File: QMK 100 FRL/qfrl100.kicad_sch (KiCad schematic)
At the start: 18 parts

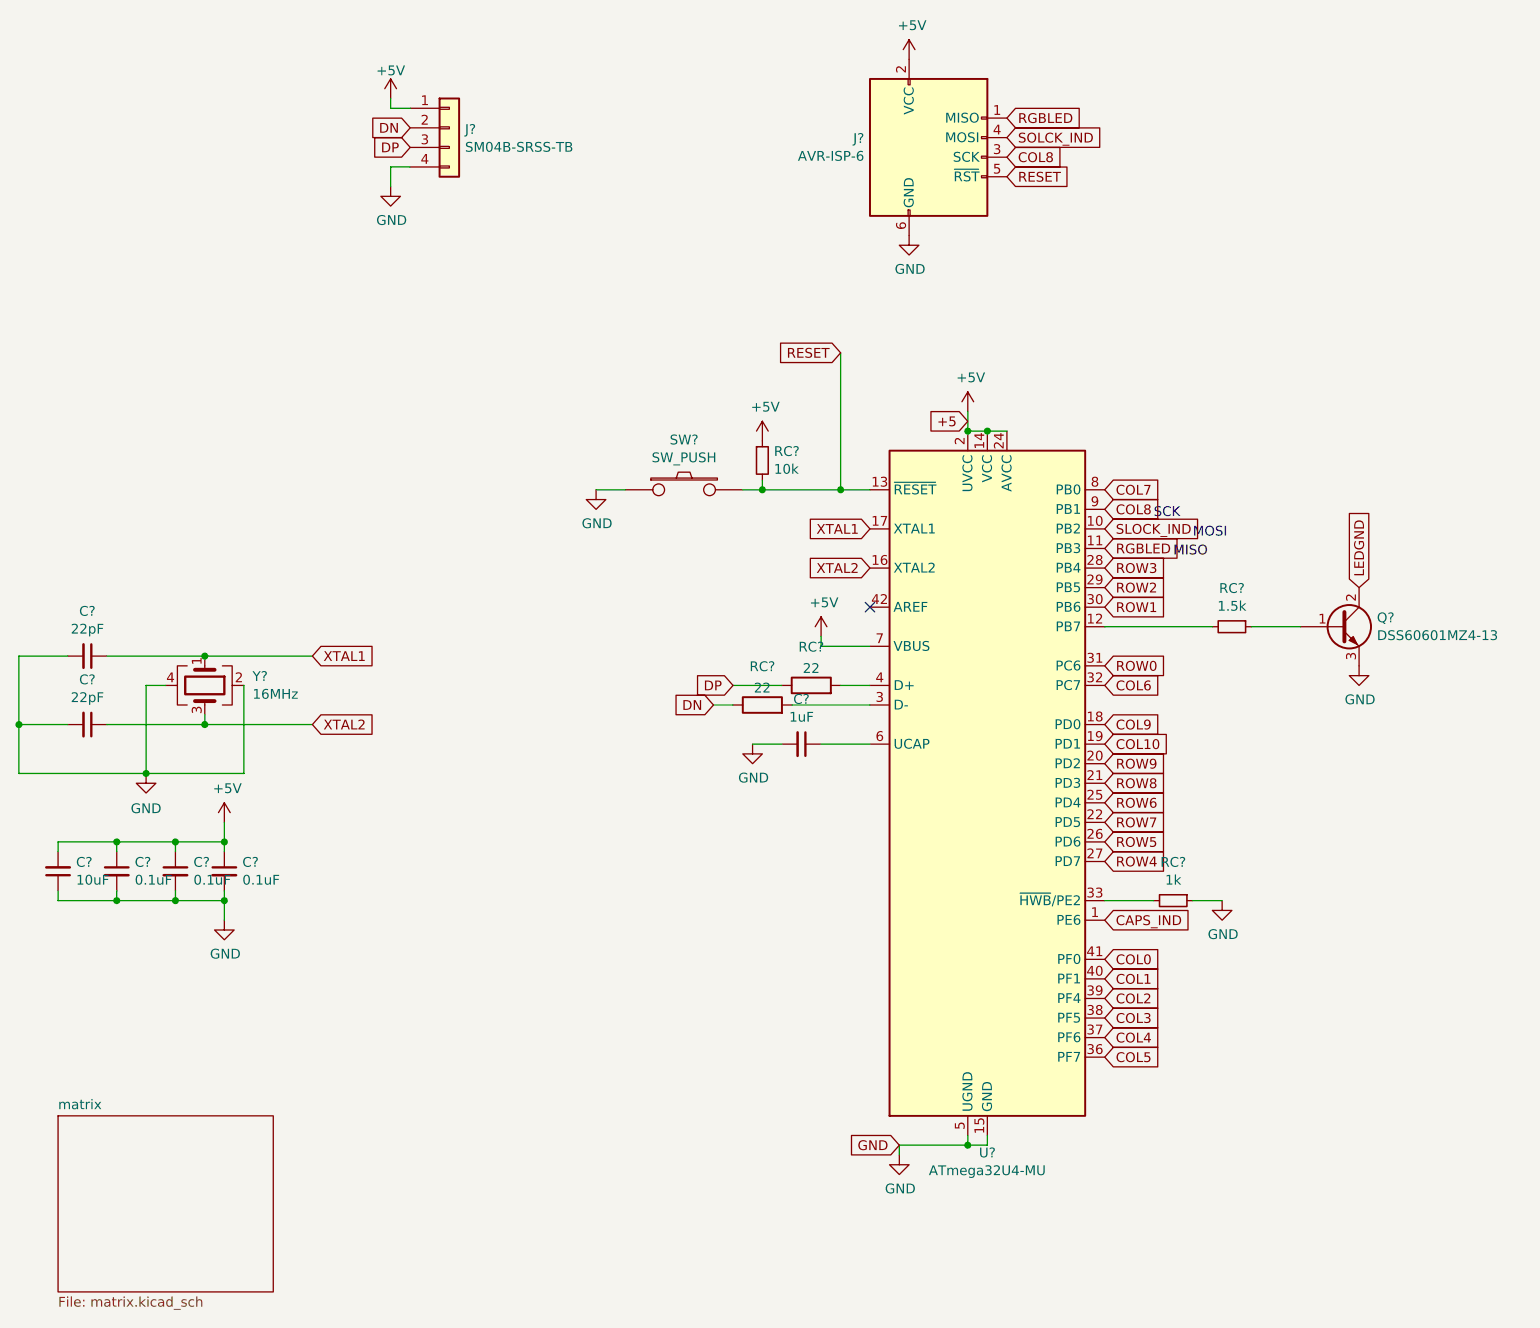
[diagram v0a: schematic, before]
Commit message: Finished from the first schema and pcb
Finished the schematics and foot prints links and updated the pcb foot prints to the pcb.
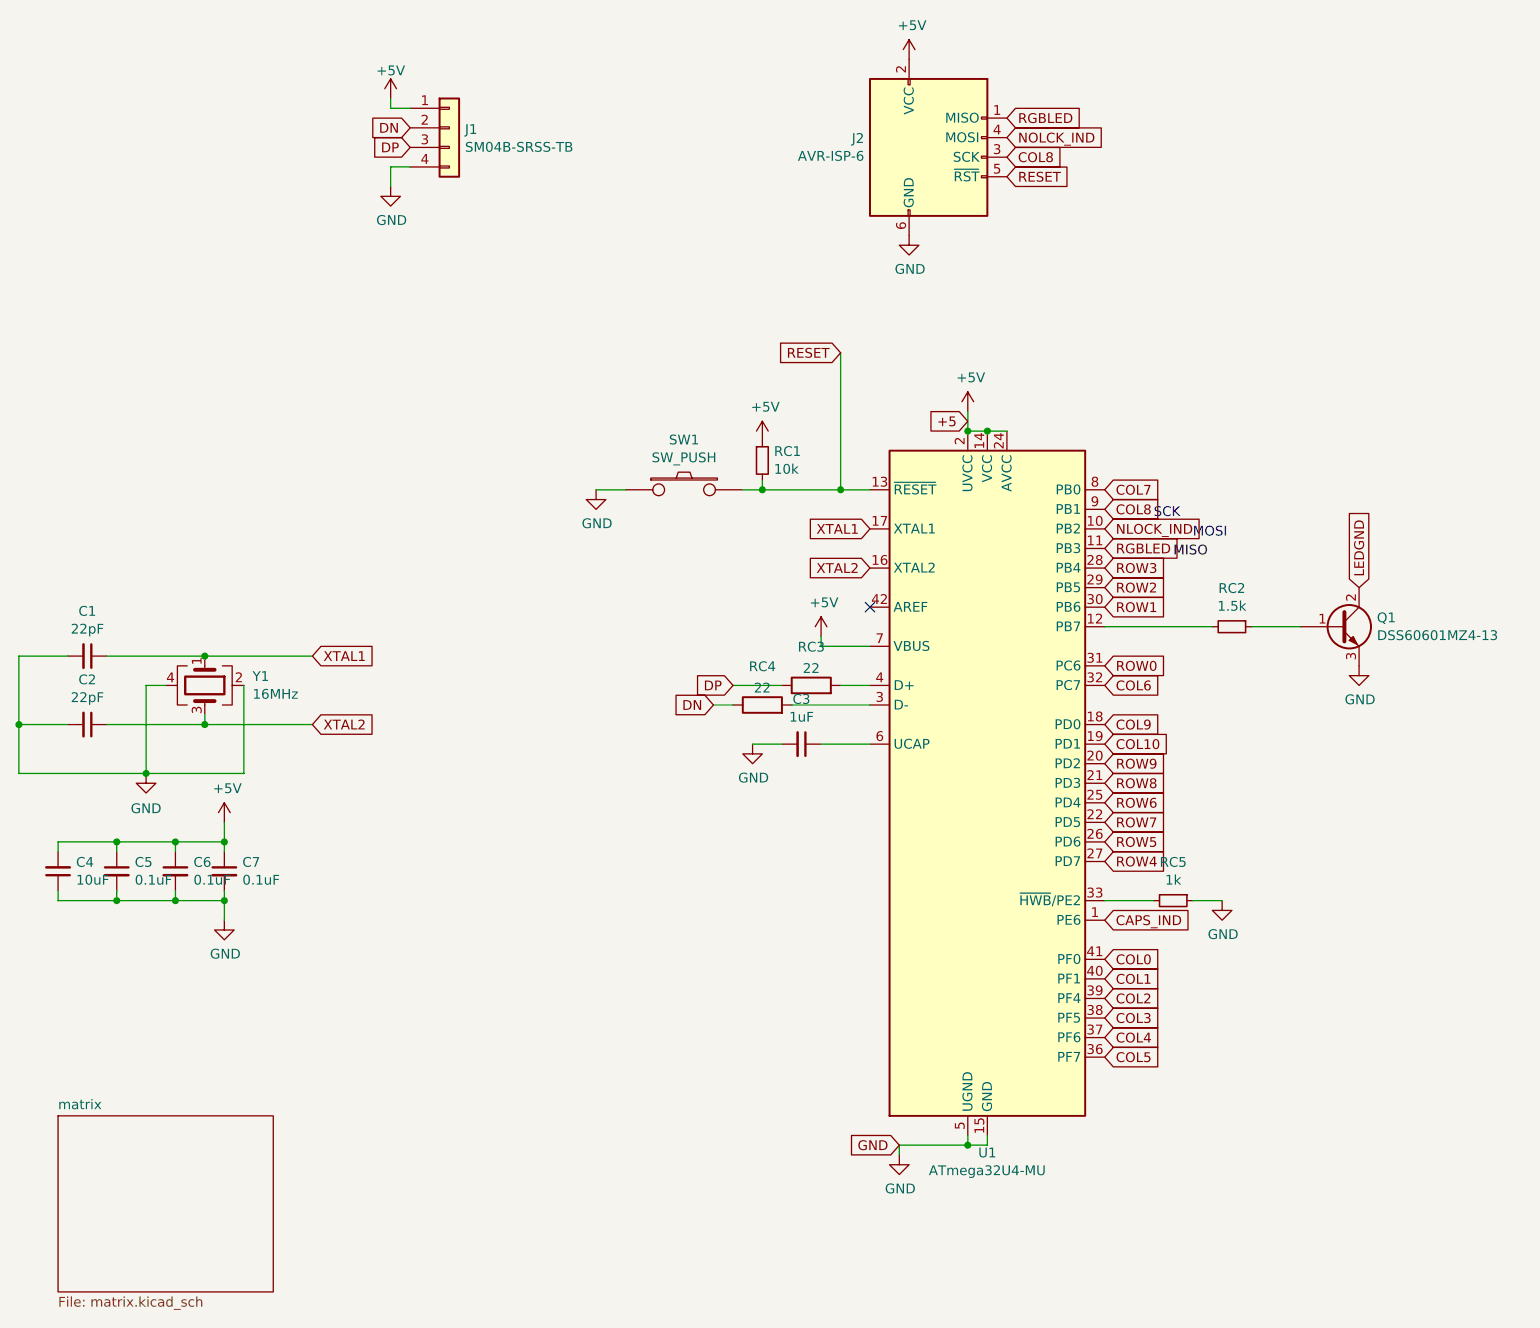
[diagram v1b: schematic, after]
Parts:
- gave numbers to parts that had none: 18
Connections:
- net SLOCK_IND renamed NLOCK_IND
- net SOLCK_IND renamed NOLCK_IND
